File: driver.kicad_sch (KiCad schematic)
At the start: 38 parts, among them Q1 SIZ322DT, Q2 SIZ322DT, Q3 SIZ322DT, U4 TMC6200

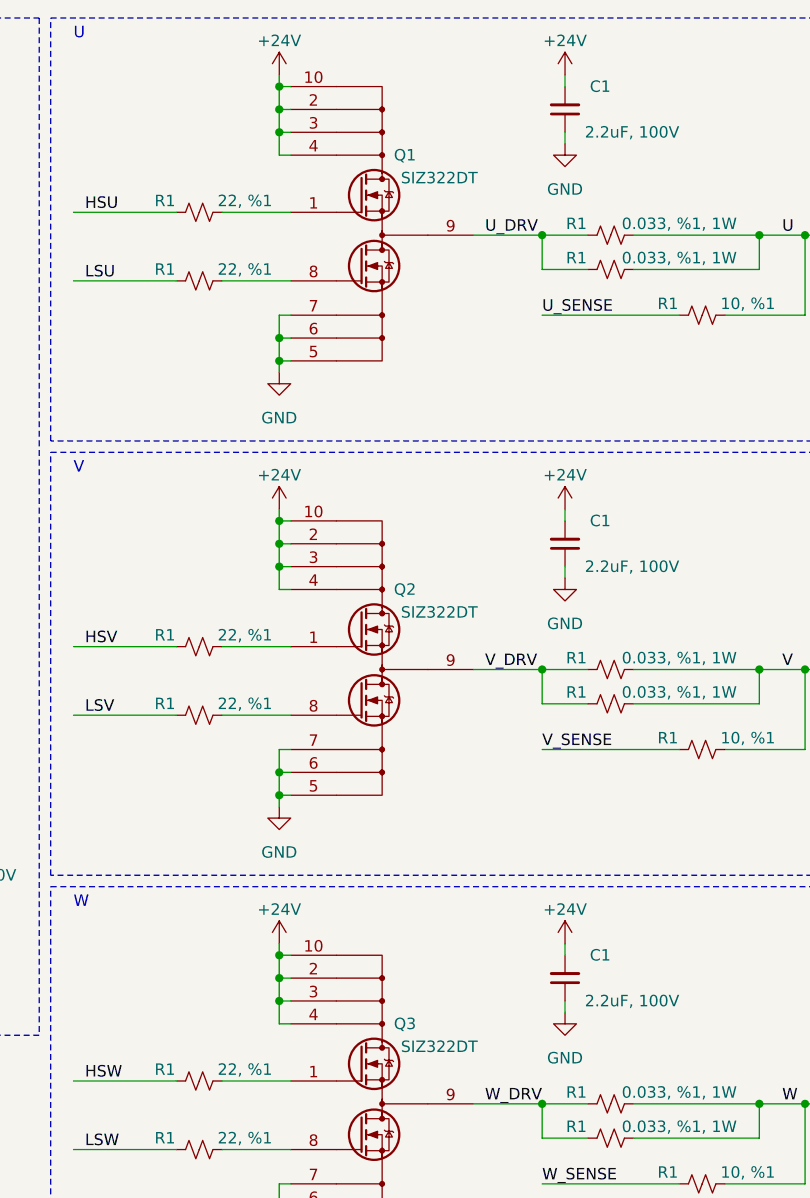
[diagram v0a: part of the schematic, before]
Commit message: Finish controller and driver schematics.
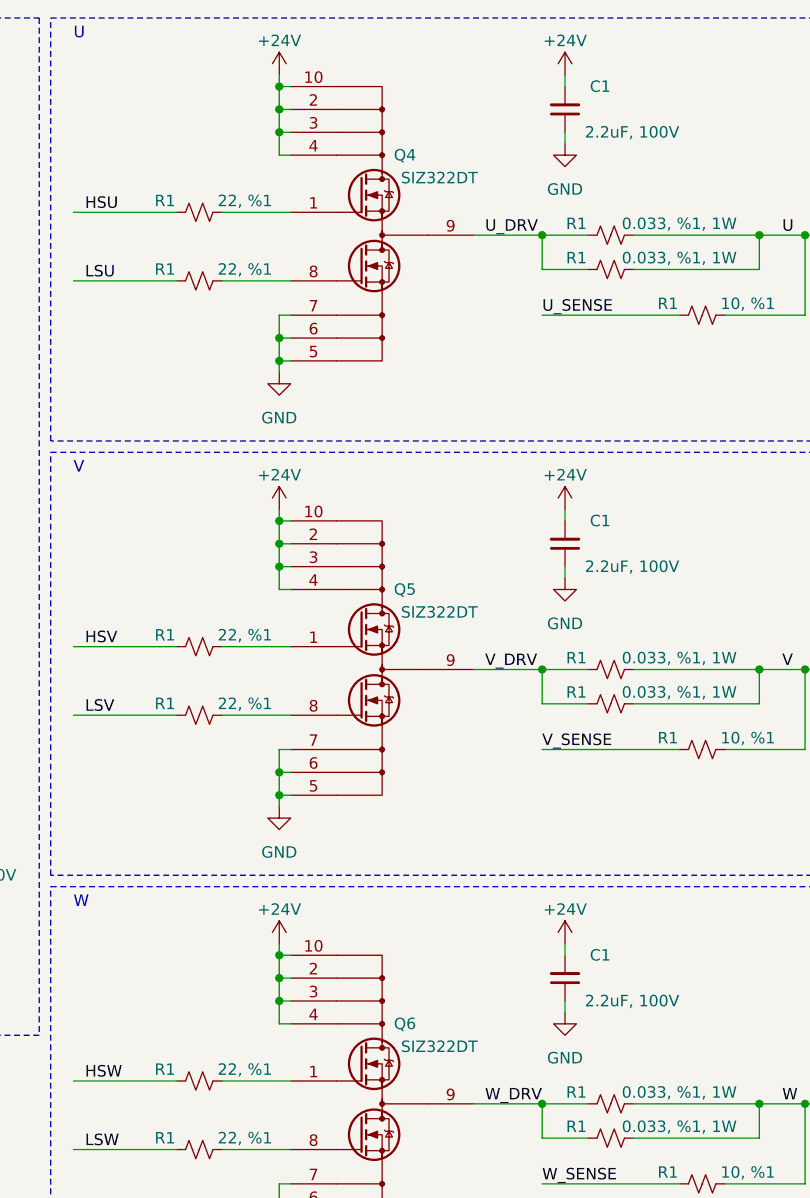
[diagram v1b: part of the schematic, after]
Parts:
- renumbered Q1 to Q4, Q2 to Q5, Q3 to Q6
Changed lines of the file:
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@@
   (symbol (lib_id "SIZ322DT-T1-GE3:SIZ322DT-T1-GE3") (at 219.71 134.62 0) (unit 1)
     (in_bom yes) (on_board yes) (dnp no)
-    (property "Reference" "Q3" (at 222.25 127 0)
+    (property "Reference" "Q6" (at 222.25 127 0)
       (effects (font (size 1.27 1.27)))
     )
@@
   (symbol (lib_id "power:+24V") (at 240.03 69.85 0) (unit 1)
     (in_bom yes) (on_board yes) (dnp no) (fields_autoplaced)
-    (property "Reference" "#PWR051" (at 240.03 73.66 0)
+    (property "Reference" "#PWR065" (at 240.03 73.66 0)
       (effects (font (size 1.27 1.27)) hide)
     )
@@
   (symbol (lib_id "power:GND") (at 208.28 102.87 0) (unit 1)
     (in_bom yes) (on_board yes) (dnp no) (fields_autoplaced)
-    (property "Reference" "#PWR050" (at 208.28 109.22 0)
+    (property "Reference" "#PWR060" (at 208.28 109.22 0)
       (effects (font (size 1.27 1.27)) hide)
     )
@@
   (symbol (lib_id "power:GND") (at 208.28 151.13 0) (unit 1)
     (in_bom yes) (on_board yes) (dnp no) (fields_autoplaced)
-    (property "Reference" "#PWR054" (at 208.28 157.48 0)
+    (property "Reference" "#PWR062" (at 208.28 157.48 0)
       (effects (font (size 1.27 1.27)) hide)
     )
@@
   (symbol (lib_id "power:GND") (at 240.03 29.21 0) (unit 1)
     (in_bom yes) (on_board yes) (dnp no) (fields_autoplaced)
-    (property "Reference" "#PWR047" (at 240.03 35.56 0)
+    (property "Reference" "#PWR064" (at 240.03 35.56 0)
       (effects (font (size 1.27 1.27)) hide)
     )
@@
   (symbol (lib_id "power:GND") (at 240.03 125.73 0) (unit 1)
     (in_bom yes) (on_board yes) (dnp no) (fields_autoplaced)
-    (property "Reference" "#PWR056" (at 240.03 132.08 0)
+    (property "Reference" "#PWR068" (at 240.03 132.08 0)
       (effects (font (size 1.27 1.27)) hide)
     )
@@
   (symbol (lib_id "power:GND") (at 240.03 77.47 0) (unit 1)
     (in_bom yes) (on_board yes) (dnp no) (fields_autoplaced)
-    (property "Reference" "#PWR052" (at 240.03 83.82 0)
+    (property "Reference" "#PWR066" (at 240.03 83.82 0)
       (effects (font (size 1.27 1.27)) hide)
     )
@@
   (symbol (lib_id "power:+24V") (at 208.28 21.59 0) (unit 1)
     (in_bom yes) (on_board yes) (dnp no) (fields_autoplaced)
-    (property "Reference" "#PWR045" (at 208.28 25.4 0)
+    (property "Reference" "#PWR057" (at 208.28 25.4 0)
       (effects (font (size 1.27 1.27)) hide)
     )
@@
   (symbol (lib_id "SIZ322DT-T1-GE3:SIZ322DT-T1-GE3") (at 219.71 38.1 0) (unit 1)
     (in_bom yes) (on_board yes) (dnp no)
-    (property "Reference" "Q1" (at 222.25 30.48 0)
+    (property "Reference" "Q4" (at 222.25 30.48 0)
       (effects (font (size 1.27 1.27)))
     )
@@
   (symbol (lib_id "power:GND") (at 208.28 54.61 0) (unit 1)
     (in_bom yes) (on_board yes) (dnp no) (fields_autoplaced)
-    (property "Reference" "#PWR048" (at 208.28 60.96 0)
+    (property "Reference" "#PWR058" (at 208.28 60.96 0)
       (effects (font (size 1.27 1.27)) hide)
     )
@@
   (symbol (lib_id "SIZ322DT-T1-GE3:SIZ322DT-T1-GE3") (at 219.71 86.36 0) (unit 1)
     (in_bom yes) (on_board yes) (dnp no)
-    (property "Reference" "Q2" (at 222.25 78.74 0)
+    (property "Reference" "Q5" (at 222.25 78.74 0)
       (effects (font (size 1.27 1.27)))
     )
@@
   (symbol (lib_id "power:+24V") (at 208.28 69.85 0) (unit 1)
     (in_bom yes) (on_board yes) (dnp no) (fields_autoplaced)
-    (property "Reference" "#PWR049" (at 208.28 73.66 0)
+    (property "Reference" "#PWR059" (at 208.28 73.66 0)
       (effects (font (size 1.27 1.27)) hide)
     )
@@
   (symbol (lib_id "power:+24V") (at 240.03 21.59 0) (unit 1)
     (in_bom yes) (on_board yes) (dnp no) (fields_autoplaced)
-    (property "Reference" "#PWR046" (at 240.03 25.4 0)
+    (property "Reference" "#PWR063" (at 240.03 25.4 0)
       (effects (font (size 1.27 1.27)) hide)
     )
@@
   (symbol (lib_id "power:+24V") (at 208.28 118.11 0) (unit 1)
     (in_bom yes) (on_board yes) (dnp no) (fields_autoplaced)
-    (property "Reference" "#PWR053" (at 208.28 121.92 0)
+    (property "Reference" "#PWR061" (at 208.28 121.92 0)
       (effects (font (size 1.27 1.27)) hide)
     )
@@
   (symbol (lib_id "power:+24V") (at 240.03 118.11 0) (unit 1)
     (in_bom yes) (on_board yes) (dnp no) (fields_autoplaced)
-    (property "Reference" "#PWR055" (at 240.03 121.92 0)
-      (effects (font (size 1.27 1.27)) hide)
-    )
+    (property "Reference" "#PWR067" (at 240.03 121.92 0)
+      (effects (font (size 1.27 1.27)) hide)
+    )

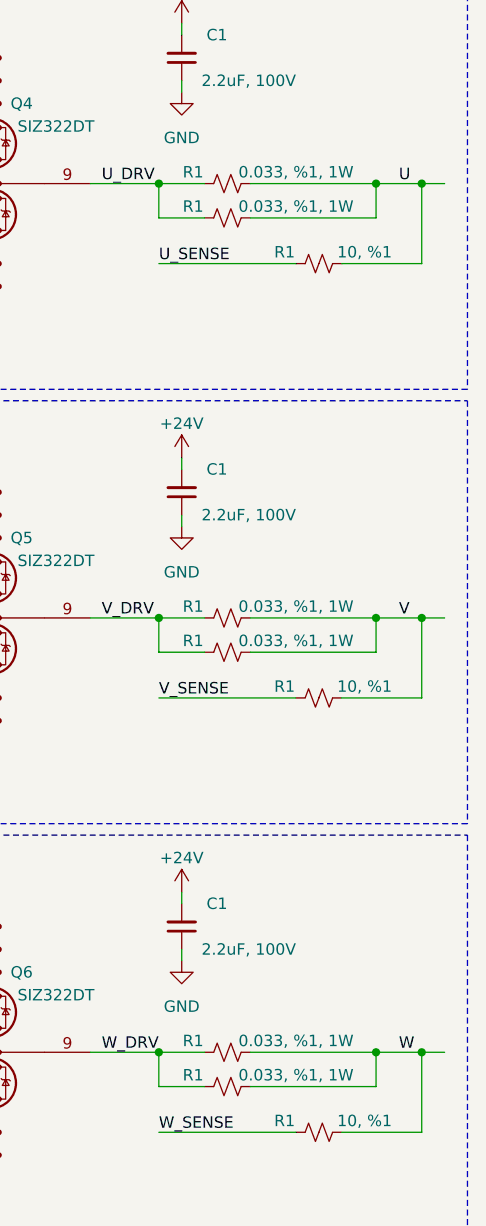
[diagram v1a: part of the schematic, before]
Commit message: Add RTMI connector.
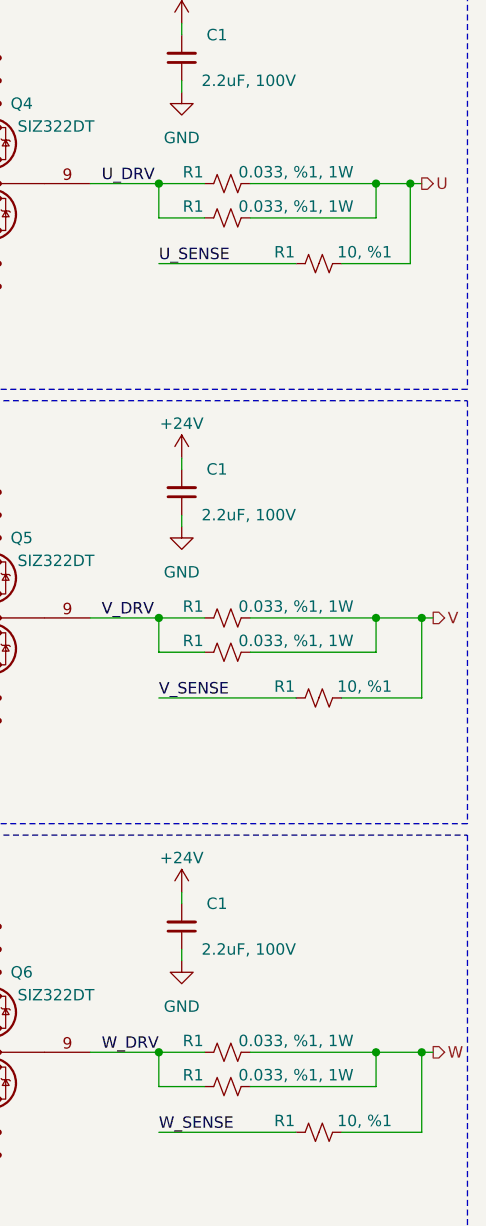
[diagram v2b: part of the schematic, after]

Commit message: Add stacking pin headers.
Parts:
- R1: footprint (none) -> Resistor_SMD:R_0603_1608Metric
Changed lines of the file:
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@@
       (effects (font (size 1.27 1.27)))
     )
-    (property "Footprint" "" (at 64.77 62.23 0)
+    (property "Footprint" "Resistor_SMD:R_0603_1608Metric" (at 64.77 62.23 0)
       (effects (font (size 1.27 1.27)) hide)
     )
@@
       (effects (font (size 1.27 1.27)))
     )
-    (property "Footprint" "" (at 64.77 67.31 0)
-      (effects (font (size 1.27 1.27)) hide)
-    )
+    (property "Footprint" "Resistor_SMD:R_0603_1608Metric" (at 64.77 67.31 0)
+      (effects (font (size 1.27 1.27)) hide)
+    )

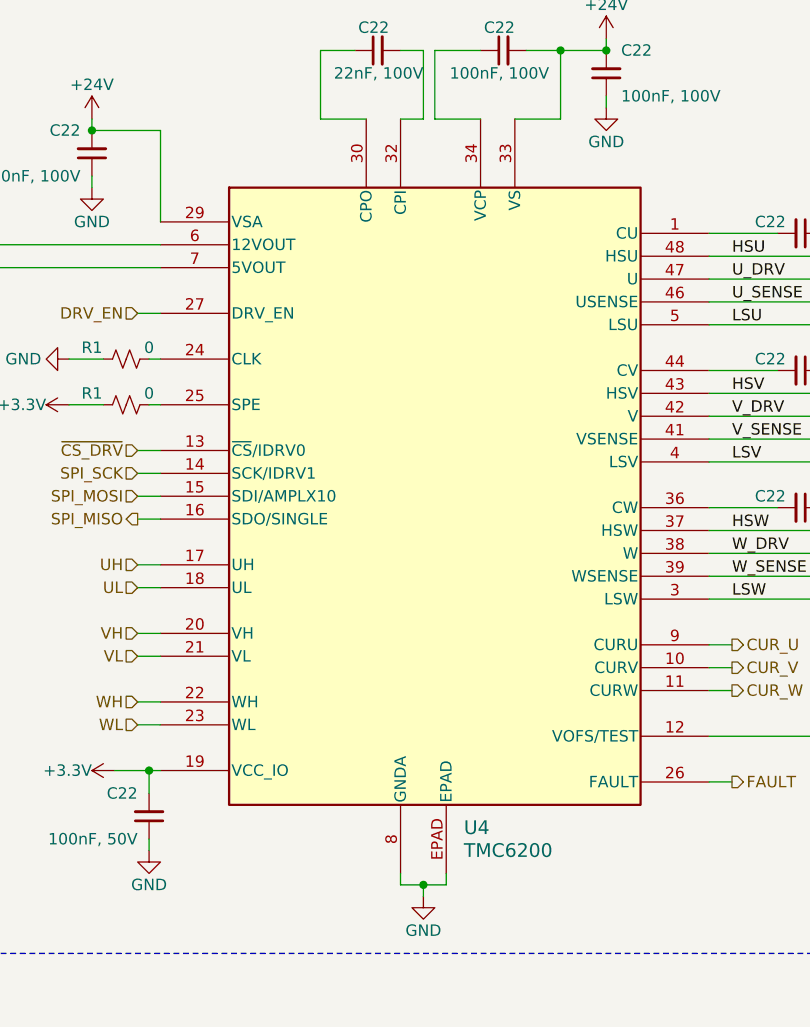
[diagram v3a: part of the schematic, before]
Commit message: Assign footprints and part numbers.
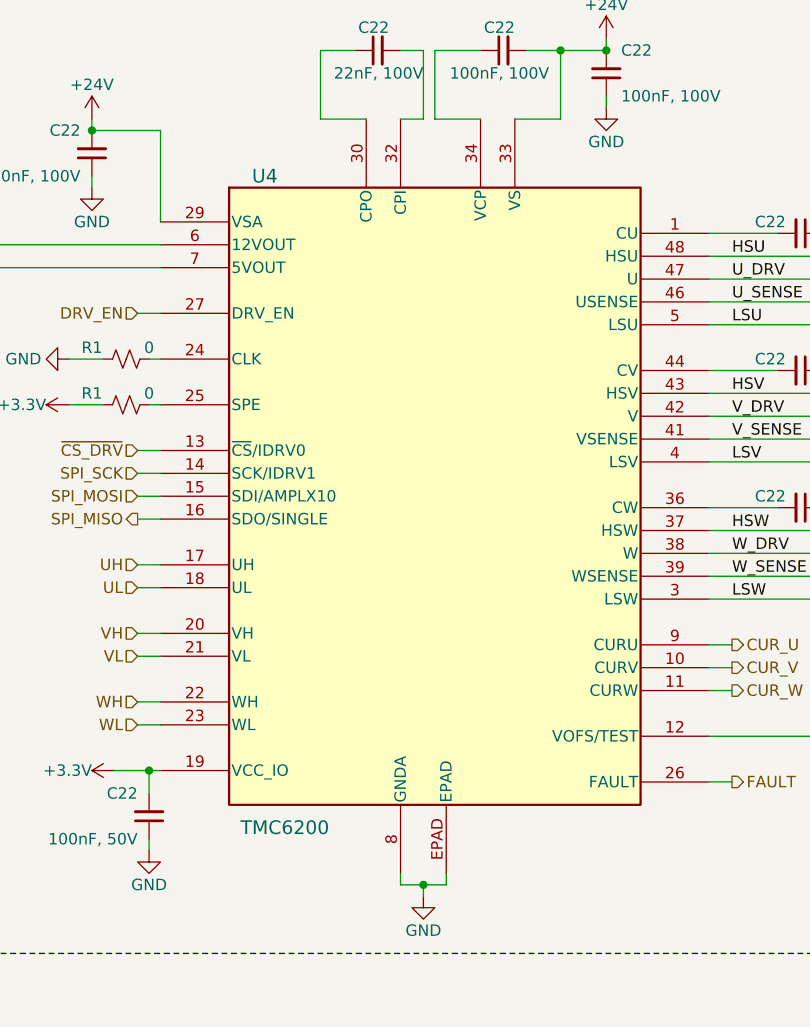
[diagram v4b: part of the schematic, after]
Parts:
- C1: footprint (none) -> Capacitor_SMD:C_1210_3225Metric; MPN (none) -> CL32B225KCJSNNE
- C22: footprint (none) -> Capacitor_SMD:C_0805_2012Metric; MPN (none) -> C2012X7R2A104K125AA
- C22: footprint (none) -> Capacitor_SMD:C_0805_2012Metric; MPN (none) -> UMK212BB7225KG-T
- C22: footprint (none) -> Capacitor_SMD:C_0603_1608Metric; MPN (none) -> C0603C103K5RAC7867
- C22: footprint (none) -> Capacitor_SMD:C_0603_1608Metric; MPN (none) -> C0603C223K1RAC7867
- C22: footprint (none) -> Capacitor_SMD:C_0603_1608Metric; MPN (none) -> C0603C474K4RAC7867
- C34: footprint (none) -> Capacitor_SMD:CP_Elec_6.3x7.7; MPN (none) -> 865080645012
- Q4, Q5, Q6: MPN (none) -> SIZ322DT-T1-GE3; Manufacturer_Part_Number SIZ322DT-T1-GE3 -> (none)
- R1: footprint (none) -> Resistor_SMD:R_0603_1608Metric; MPN (none) -> ERJ-3EKF22R0V
- R1: footprint (none) -> Resistor_SMD:R_0603_1608Metric; MPN (none) -> ERJ-3EKF10R0V
- R1: footprint (none) -> Resistor_SMD:R_1206_3216Metric; MPN (none) -> ERJ-8CWFR033V
- R1: MPN (none) -> ERJ-3GEY0R00V
- R4: footprint (none) -> Resistor_SMD:R_0603_1608Metric; MPN (none) -> ERJ-3EKF1501V
- R4: footprint (none) -> Resistor_SMD:R_0603_1608Metric; MPN (none) -> ERJ-3EKF4701V
- U4: MPN (none) -> TMC6200-TA

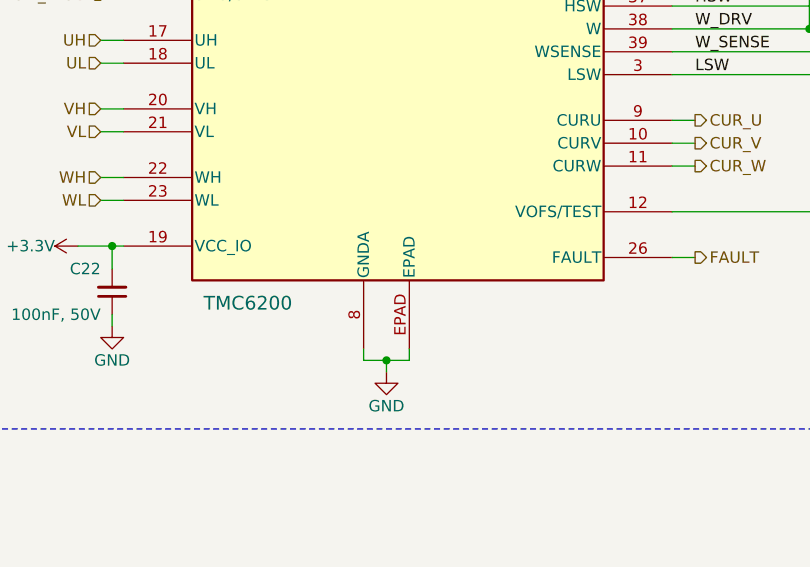
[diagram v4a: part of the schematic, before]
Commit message: Finish the initial placement, switch most of the parts to 0402.
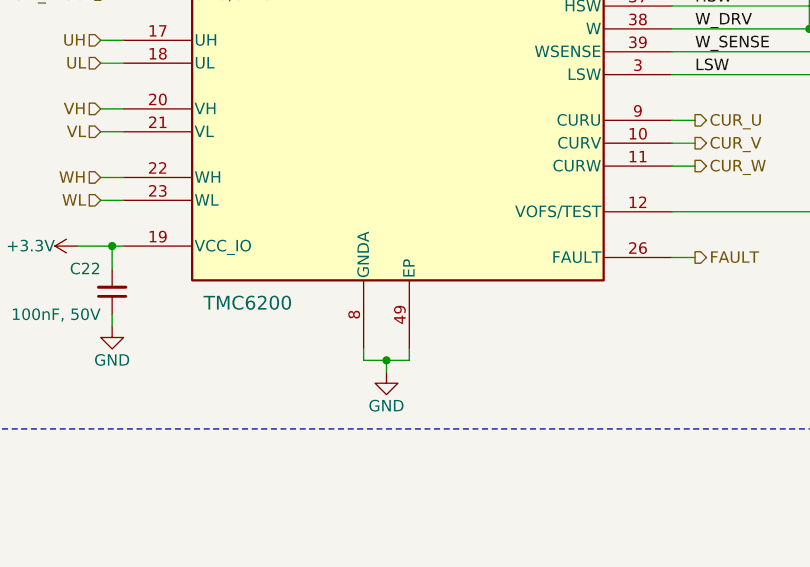
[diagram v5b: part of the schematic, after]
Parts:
- C1: footprint Capacitor_SMD:C_1210_3225Metric -> Capacitor_SMD:C_1206_3216Metric; MPN CL32B225KCJSNNE -> CL31B225KCHSNNE
- C22: footprint Capacitor_SMD:C_0805_2012Metric -> Capacitor_SMD:C_0603_1608Metric; MPN C2012X7R2A104K125AA -> CL10B104KC8NNNC
- C22: footprint Capacitor_SMD:C_0603_1608Metric -> Capacitor_SMD:C_0402_1005Metric; MPN C0603C103K5RAC7867 -> CL05B104KB54PNC
- R1: footprint Resistor_SMD:R_0603_1608Metric -> Resistor_SMD:R_0402_1005Metric; MPN ERJ-3EKF22R0V -> ERJ-2RKF22R0X
- R1: footprint Resistor_SMD:R_0603_1608Metric -> Resistor_SMD:R_0402_1005Metric; MPN ERJ-3EKF10R0V -> ERJ-2RKF10R0X
- R1: footprint Resistor_SMD:R_0603_1608Metric -> Resistor_SMD:R_0402_1005Metric; MPN ERJ-3GEY0R00V -> ERJ-2GE0R00X
- R4: footprint Resistor_SMD:R_0603_1608Metric -> Resistor_SMD:R_0402_1005Metric; MPN ERJ-3EKF1501V -> ERJ-2RKF1501X
- R4: footprint Resistor_SMD:R_0603_1608Metric -> Resistor_SMD:R_0402_1005Metric; MPN ERJ-3EKF4701V -> ERJ-2RKF4701X
- U4: footprint TMC6200:eTQFP48_9x9_TRI -> Package_QFP:TQFP-48-1EP_7x7mm_P0.5mm_EP5x5mm
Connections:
- net GND: now also U4.49 (EP); no longer U4.EPAD
